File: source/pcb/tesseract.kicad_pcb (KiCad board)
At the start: 2 copper layers, 83 parts, among them J1 USB_C_Receptacle_USB2.0_14P, J2 AudioJack3_SwitchTR, J3 Conn_01x12, J4 Conn_01x02, J5 Micro_SD_Card_Det1, SW1 SW_Push, SW2 SW_Push, SW3 SW_Push, SW4 SW_Push, SW5 SW_Push, SW6 SW_Push, U1 PCM5102A, U2 IP5306, U3 RP2354A, U4 XC6206PxxxMR, U5 PAM8403D, Y1 Crystal_GND24

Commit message: Created PCB layout
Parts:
- removed SW5, SW6: SW_Push, Button_Switch_SMD:SW_Push_1P1T_NO_CK_PTS125Sx43PSMTR
- C1, C10, C11, C12, C13, C14, C15, C16, C17, C18, C19, C2, C20, C21, C22, C23, C24, C25, C26, C27, C28, C29, C3, C30, C31, C32, C33, C34, C35, C36, C37, C38, C39, C4, C40, C41, C42, C43, C5, C6, C7, C8, C9, J1, J2, J3, J5, L1, L2, R1, R10, R11, R12, R13, R14, R15, R16, R17, R18, R2, R3, R4, R5, R6, R7, R8, R9, U1, U2, U3, U4, U5, U6, Y1: moved to B.Cu
- SW1, SW2: footprint footprints:button_342 -> Inductor_SMD:L_Taiyo-Yuden_NR-40xx; moved to B.Cu
- SW3, SW4: footprint Button_Switch_SMD:SW_Push_1P1T_NO_CK_PTS125Sx43PSMTR -> footprints:button_342
- moved C10 143.1 mm to (171.2, 117.0), turned to -90 degrees
- moved C9 135.4 mm to (170.1, 117.0), turned to -90 degrees
- moved SW4 129.9 mm to (171.5, 80.5)
- moved C23 128.9 mm to (156.2, 117.9), turned to 180 degrees
- moved C25 128.3 mm to (158.9, 118.0), turned to 180 degrees
- moved C26 126.9 mm to (159.7, 116.8), turned to 180 degrees
- moved J4 125.0 mm to (164.4, 121.8), turned to 90 degrees
- moved C24 124.9 mm to (159.8, 109.7), turned to 180 degrees
- moved J1 119.1 mm to (148.6, 131.0), turned to 180 degrees
- moved L2 117.1 mm to (161.3, 117.0), turned to -90 degrees
- moved R1 114.1 mm to (149.4, 124.8), turned to 90 degrees
- moved C12 113.7 mm to (154.8, 91.4)
- moved C41 112.1 mm to (143.9, 112.3), turned to 90 degrees
- moved C13 111.8 mm to (154.8, 89.9)
- moved C42 111.8 mm to (153.3, 104.0), turned to -90 degrees
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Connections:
- net VREG_FB renamed +1V1
- C3 pad 1: VREG_AVDD -> Net-(C3-Pad1)
- C43 pad 1: unconnected-(C43-Pad1) -> +3V3
- C43 pad 2: unconnected-(C43-Pad2) -> GND
- R5 pad 2: VREG_AVDD -> Net-(C3-Pad1)
- U3 pad 14: B3 -> unconnected-(U3-GPIO10-Pad14)
- U3 pad 15: B4 -> unconnected-(U3-GPIO11-Pad15)
- U3 pad 46: VREG_AVDD -> +3V3
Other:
- board outline added: 65 x 100 mm
- copper layers 2 -> 4

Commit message: Routed PCB signals
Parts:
- moved C40 26.6 mm to (137.3, 119.5), turned to 0 degrees
- moved R13 16.6 mm to (139.9, 119.5), turned to 0 degrees
- moved C3 16.0 mm to (146.7, 87.9)
- moved C43 7.00 mm to (159.2, 56.6)
- moved J3 7.00 mm to (162.7, 57.8)
- moved R14 7.00 mm to (159.2, 54.6)
- moved C38 1.02 mm to (137.5, 106.2)
- moved C37 1.00 mm to (137.5, 107.2)
- moved U6 0.50 mm to (149.1, 103.5)
- moved C31 0.24 mm to (134.6, 95.9)
- moved C30 0.18 mm to (136.5, 95.9)
- moved SW2 0.18 mm to (145.3, 76.4)
- moved C29 0.12 mm to (138.3, 95.9)
- moved L1 0.10 mm to (146.7, 89.0)
- moved C28 0.06 mm to (140.1, 95.9)
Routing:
- net LCDDC: track 0.00 -> 44.9 mm
- net LCDCS: track 0.00 -> 44.5 mm, vias 0 -> 2
- net LCDSCL: track 0.00 -> 44.2 mm, vias 0 -> 2
- net USB D+: track 0.00 -> 43.0 mm, vias 0 -> 2
- net USB D-: track 0.00 -> 43.0 mm, vias 0 -> 2
- net LCDSDA: track 0.00 -> 42.2 mm, vias 0 -> 2
- net SDCD: track 0.00 -> 41.9 mm, vias 0 -> 2
- net DACOUTR: track 0.00 -> 38.5 mm, vias 0 -> 2
- net LCDRST: track 0.00 -> 38.2 mm
- net SDSCK: track 0.00 -> 37.9 mm, vias 0 -> 2
- net unconnected-(J5-SHIELD-PadSH): track 0.00 -> 37.4 mm
- net SDMOSI: track 0.00 -> 36.8 mm, vias 0 -> 2
- net SDMISO: track 0.00 -> 36.0 mm, vias 0 -> 2
- net BCK: track 0.00 -> 35.9 mm, vias 0 -> 4
- net B2: track 0.00 -> 34.6 mm, vias 0 -> 1
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
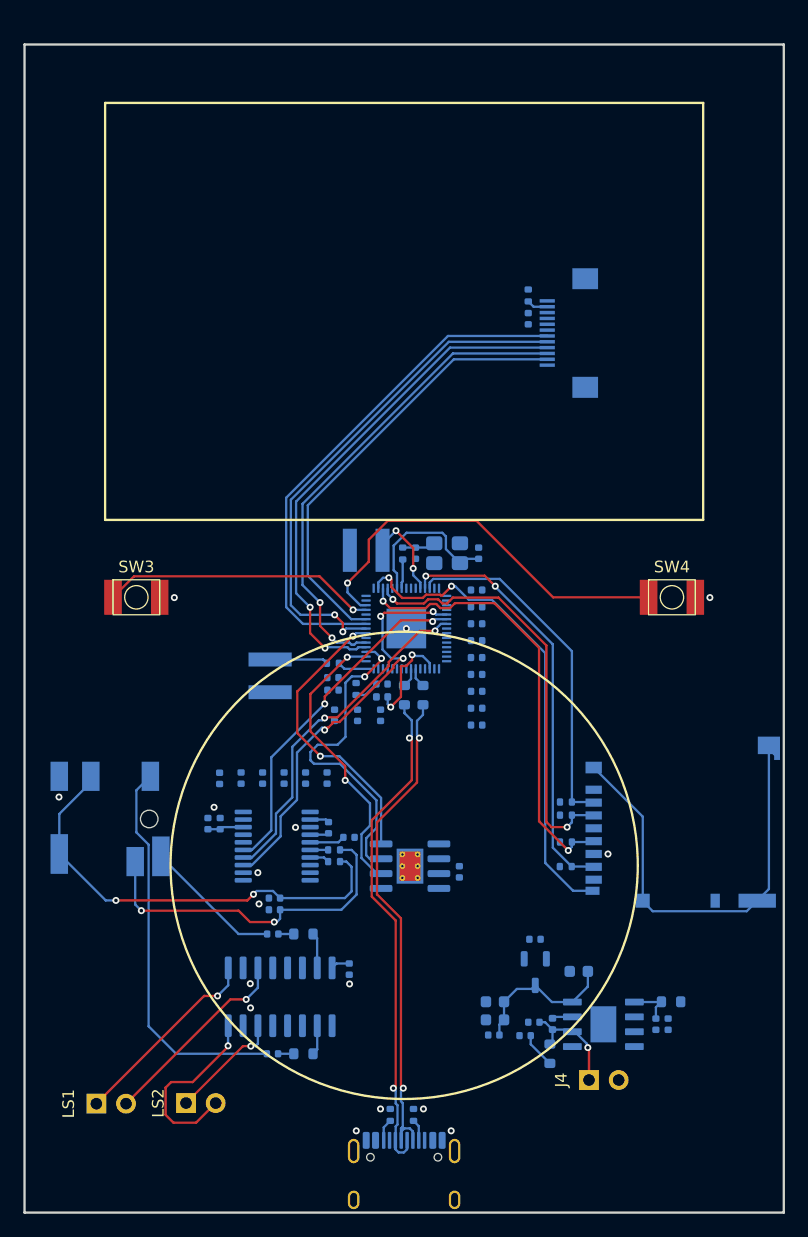
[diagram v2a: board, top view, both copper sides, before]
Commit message: Finished PCB routing
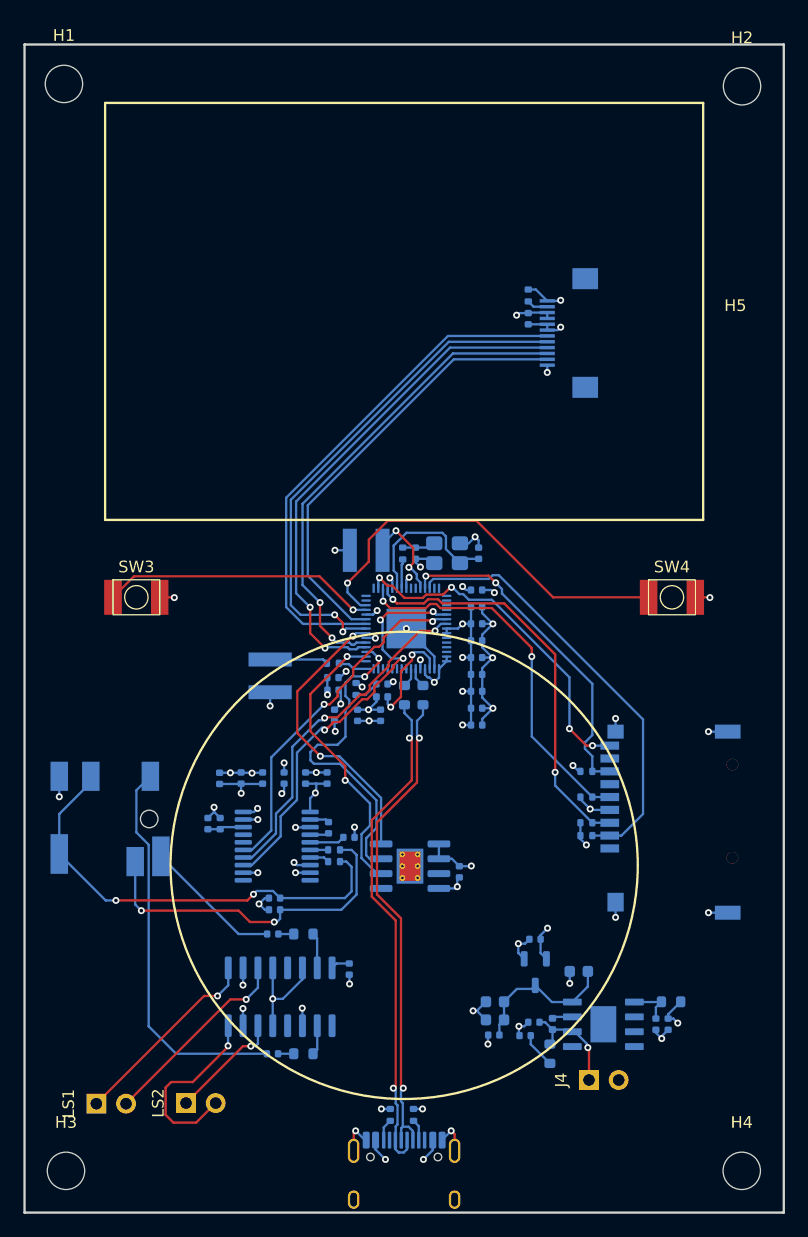
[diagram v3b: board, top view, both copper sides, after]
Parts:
- added H1: MountingHole, MountingHole:MountingHole_3.2mm_M3, F.Cu at (119.5, 36.5)
- added H2: MountingHole, MountingHole:MountingHole_3.2mm_M3, F.Cu at (177.5, 36.7)
- added H3: MountingHole, MountingHole:MountingHole_3.2mm_M3, F.Cu at (119.6, 129.6)
- added H4: MountingHole, MountingHole:MountingHole_3.2mm_M3, F.Cu at (177.5, 129.6)
- added H5: MountingHole, footprints:display_hole, F.Cu at (176.9, 56.0)
- J5: footprint Connector_Card:microSD_HC_Hirose_DM3BT-DSF-PEJS -> footprints:TF-SMD_TF-CARD-H1.8
- moved R18 8.34 mm to (164.2, 95.3)
- moved R17 4.23 mm to (164.2, 97.5)
- moved R15 3.37 mm to (164.2, 100.8)
- moved R16 1.87 mm to (164.2, 99.8)
- moved J5 1.20 mm to (171.2, 99.7)
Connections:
- J5 pad SH: unconnected-(J5-SHIELD-PadSH) -> GND
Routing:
- net +3V3: track 0.00 -> 232.3 mm, vias 0 -> 24
- net GND: track 0.00 -> 92.7 mm, vias 1 -> 49
- net VBUS: track 0.00 -> 38.6 mm, vias 0 -> 3
- net unconnected-(J5-SHIELD-PadSH): track 37.4 -> 0.00 mm
- net +1V1: track 0.00 -> 16.9 mm, vias 0 -> 3
- net SDCD: track 41.9 -> 29.9 mm, vias 2 -> 4
- net SDCS: track 30.2 -> 37.3 mm
- net SDMISO: track 36.0 -> 28.9 mm
- net SDSCK: track 37.9 -> 32.2 mm
- net SDMOSI: track 36.8 -> 34.5 mm
- net USB D-: track 43.0 -> 42.0 mm
- net LCK: track 29.7 -> 30.2 mm
- net (no net): vias 15 -> 0
- added copper zone on In1.Cu, net GND

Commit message: Added missing hours
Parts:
- added G***: LOGO, LOGO, B.Cu at (148.6, 56.0)
- moved U6 0.50 mm to (148.6, 103.5)
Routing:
- net WHLSCL: track 28.0 -> 31.5 mm, vias 2 -> 4
- net WHLSDA: track 24.9 -> 27.7 mm, vias 2 -> 4
- net WHLDIR: track 24.9 -> 27.4 mm
- net DACOUTL: track 29.7 -> 27.6 mm
- net DACOUTR: track 38.5 -> 36.6 mm
- net VBUS: track 38.6 -> 39.2 mm
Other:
- board text added: "Tesseract"

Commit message: Created first prototype of case
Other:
- board text added: "made with <3 by hridhaan shetty!"

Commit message: Added slide switch and created firmware
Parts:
- added SW5: SW_SPDT, common_footprints:SW-TH_MSK12D18G2, F.Cu at (178.4, 116.0)
- H5: footprint footprints:display_hole -> common_footprints:display_hole
- J2: footprint footprints:PJ31060 -> common_footprints:PJ31060
- J5: footprint footprints:TF-SMD_TF-CARD-H1.8 -> common_footprints:TF-SMD_TF-CARD-H1.8
- U2: footprint footprints:eSOP-8 -> common_footprints:eSOP-8
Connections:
- C24 pad 1: +3V3 -> Net-(SW5-B)
- U3 pad 15: unconnected-(U3-GPIO11-Pad15) -> SDCD
- U3 pad 16: unconnected-(U3-GPIO12-Pad16) -> SDMISO
- U3 pad 17: SDCD -> SDCS
- U3 pad 27: SDMISO -> unconnected-(U3-GPIO16-Pad27)
- U3 pad 28: SDCS -> unconnected-(U3-GPIO17-Pad28)
- U4 pad 2: +3V3 -> Net-(SW5-B)
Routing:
- net SDCS: track 37.3 -> 61.4 mm, vias 0 -> 2
- net SDMISO: track 28.9 -> 51.6 mm, vias 2 -> 5
- net Net-(SW5-B): track 0.00 -> 22.3 mm
- net +3V3: track 232.3 -> 248.6 mm, vias 24 -> 23
- net SDCD: track 29.9 -> 34.1 mm
- net GND: track 92.7 -> 94.1 mm, vias 49 -> 50
- net B2: track 34.6 -> 35.7 mm

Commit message: Added BOM
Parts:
- J2: footprint common_footprints:PJ31060 -> common_footprints:AUDIO-SMD_PJ-242_1
- moved J2 1.70 mm to (121.7, 99.4)
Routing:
- net DACOUTL: track 27.6 -> 36.3 mm
- net JACKL: track 11.8 -> 18.9 mm
- net JACKR: track 33.4 -> 26.5 mm
- net DACOUTR: track 36.6 -> 35.3 mm
